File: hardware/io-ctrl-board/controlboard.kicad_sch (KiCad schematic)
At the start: 45 parts

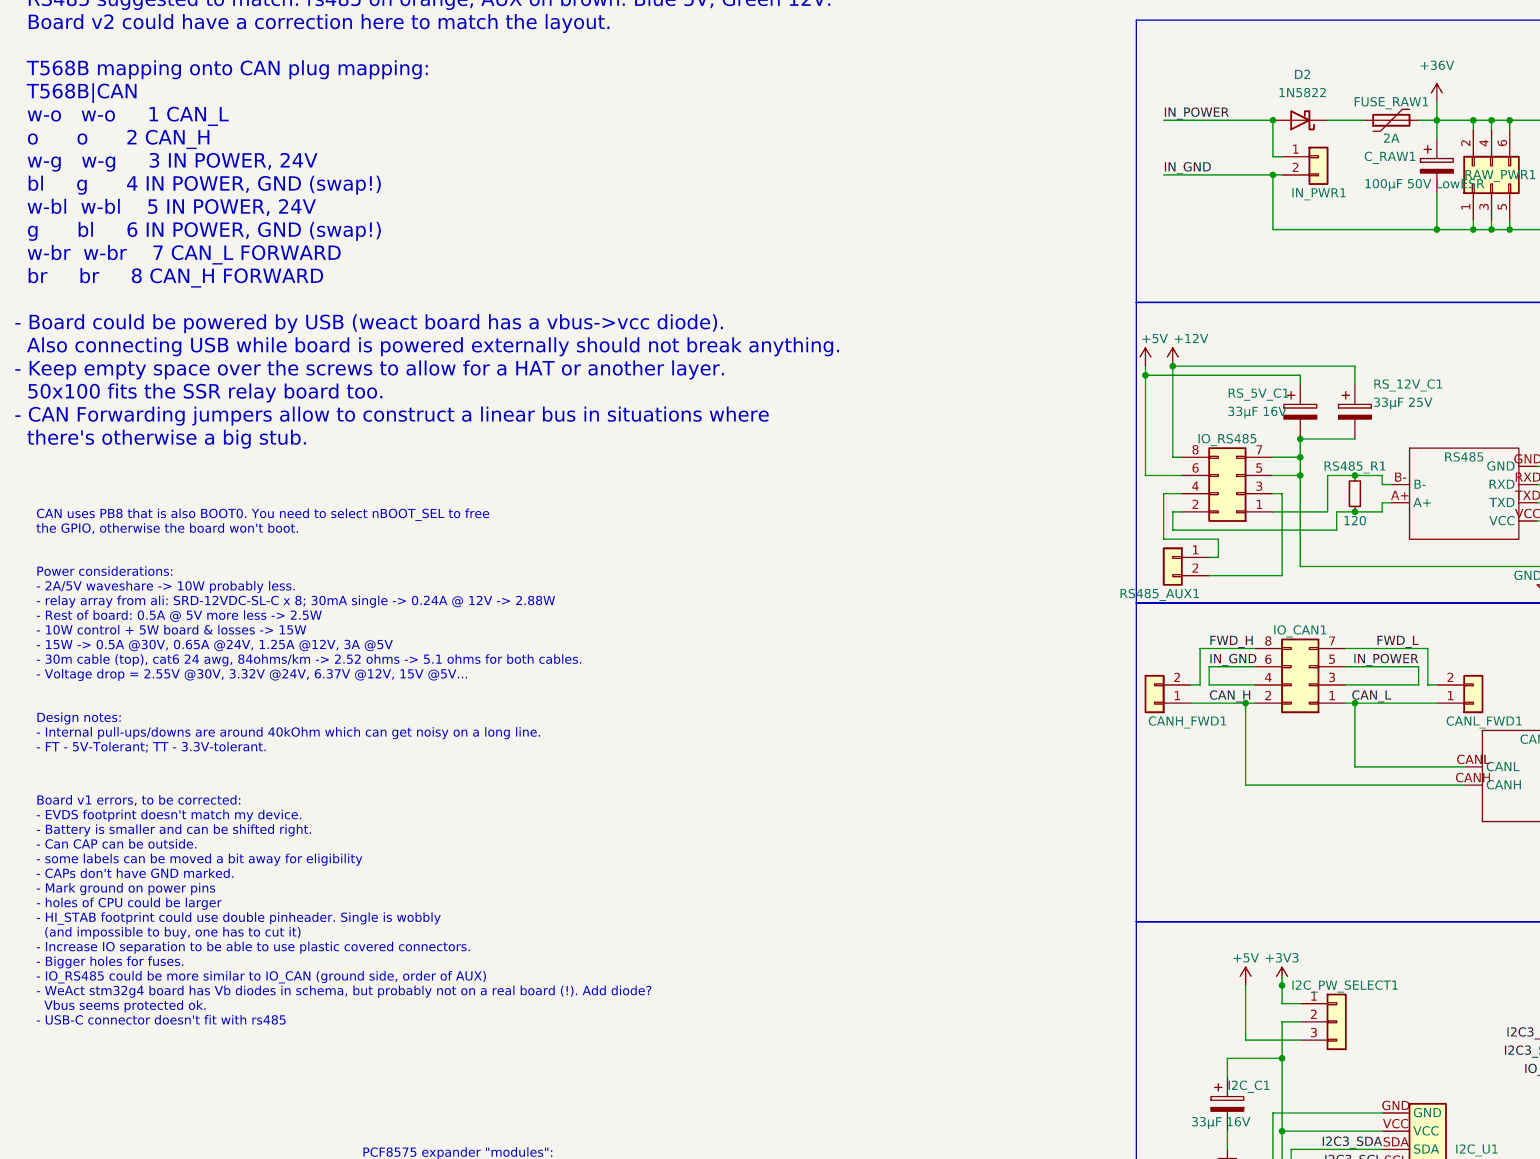
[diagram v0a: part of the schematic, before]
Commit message: Some old changes to controlboard.
There should be no true changes though. It's still v1 (one I've deployed). Board
has too little holes for fuse, otherwise is fine.
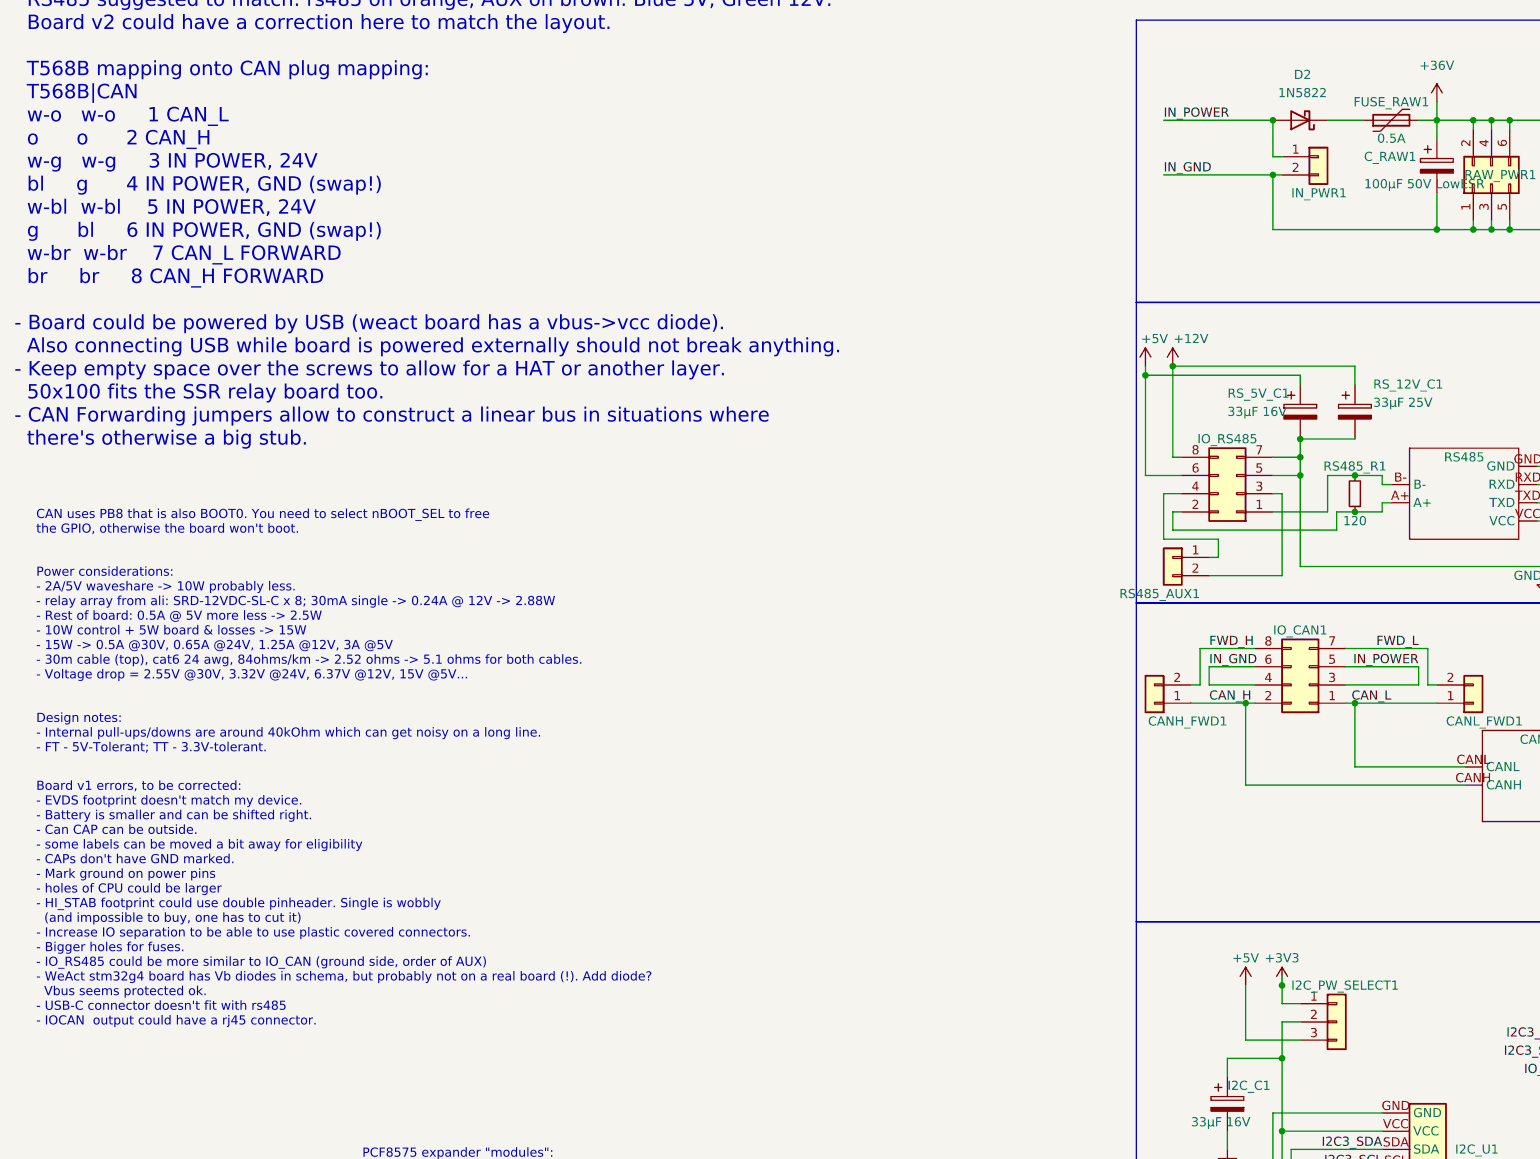
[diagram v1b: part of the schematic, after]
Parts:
- FUSE_RAW1: value 2A -> 0.5A
